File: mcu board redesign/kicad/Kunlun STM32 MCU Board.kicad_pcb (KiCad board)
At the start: 2 copper layers, 40 x 40 mm, 36 parts, among them J1 0532610671, J2 10129383-908001ALF, J3 USB4105-GF-A, J4 5002, J5 5002, J6 5002, J7 5002, J8 5001, J9 5001, SW1 KMR231NG ULC LFS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

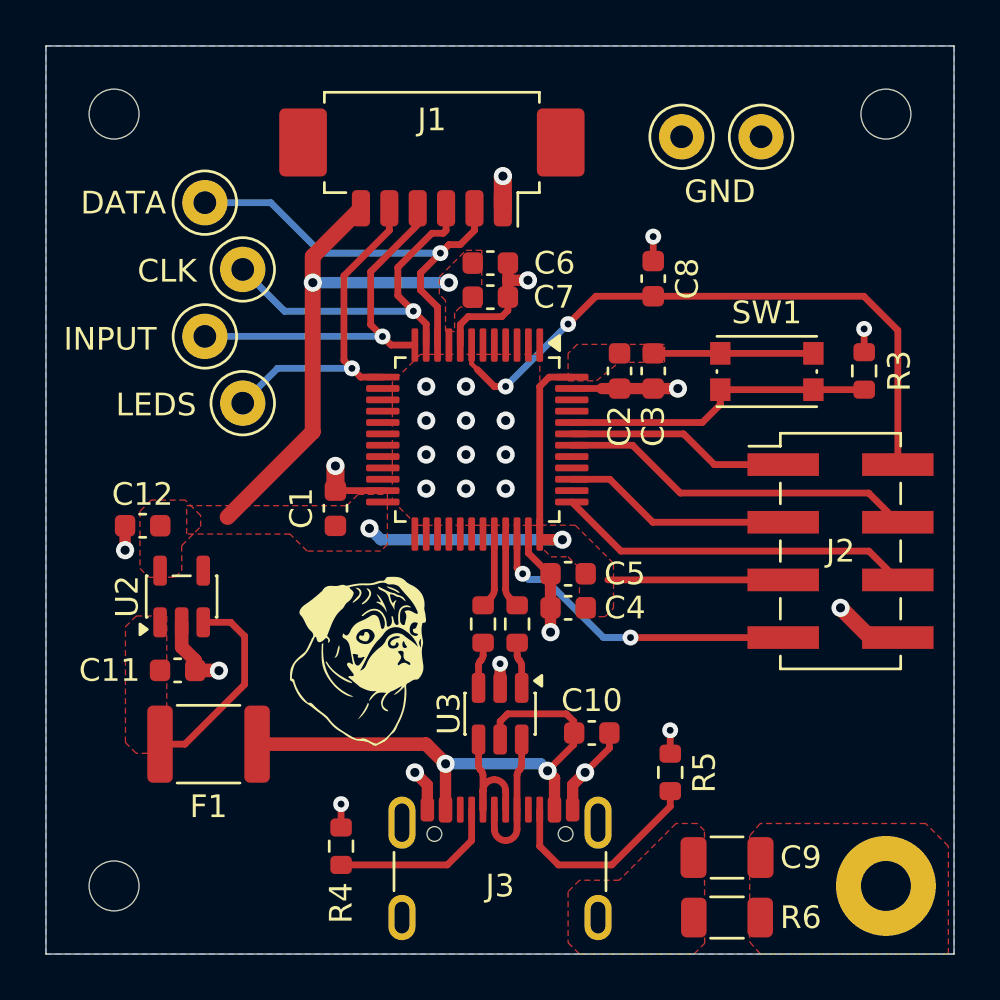
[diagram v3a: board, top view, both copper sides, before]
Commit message: More pretty things
Curve the fill around chassis ground mounting hole.
Label switch as "BOOT"
Pretty up R4
Small trace tweaks
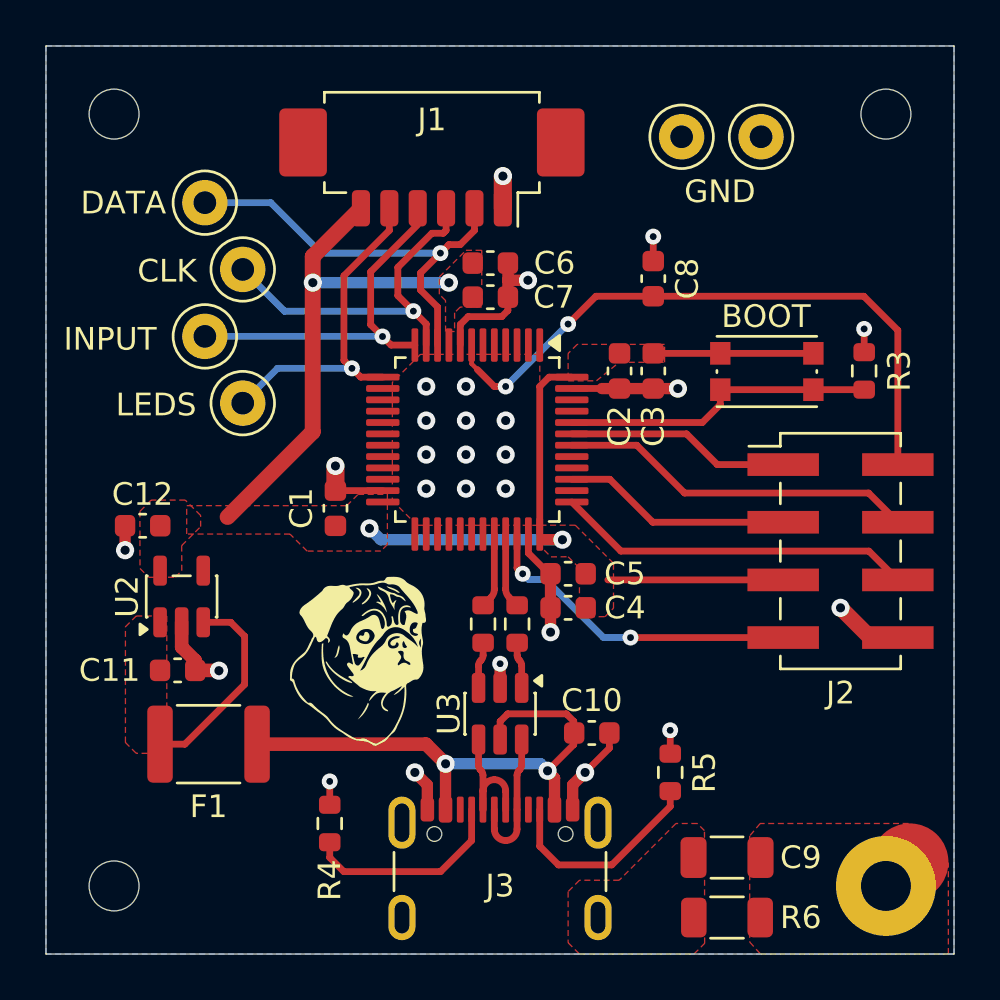
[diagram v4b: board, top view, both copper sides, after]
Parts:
- moved R4 1.12 mm to (140.8, 119.0)
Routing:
- net Net-(J3-CC1): track 7.56 -> 9.11 mm
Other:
- board text added: "BOOT"
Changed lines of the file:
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@@
 		(tags "Surface mounted pin header SMD 2x04 2.54mm double row")
 		(property "Reference" "J2"
-			(at 0 0 0)
+			(at 0 6.25 0)
 			(layer "F.SilkS")
 			(effects
@@
 	(footprint "Resistor_SMD:R_0603_1608Metric"
 		(layer "F.Cu")
-		(at 141.25 120 90)
+		(at 140.75 119 90)
 		(descr "Resistor SMD 0603 (1608 Metric), square (rectangular) end terminal, IPC-7351 nominal, (Body size source: IPC-SM-782 page 72, https://www.pcb-3d.com/wordpress/wp-content/uploads/ipc-sm-782a_amendment_1_and_2.pdf)")
 		(tags "resistor")
@@
 			(at -0.004838 -2.590547 180)
 			(layer "F.SilkS")
+			(hide yes)
 			(effects
 				(font
@@
 		)
 	)
+	(gr_circle
+		(center 166.303358 120.696583)
+		(end 167.903358 120.696583)
+		(stroke
+			(width 0.2)
+			(type solid)
+		)
+		(fill yes)
+		(layer "F.Cu")
+		(net "Net-(C9-Pad1)")
+	)
 	(gr_poly
 		(pts
@@
 		)
 	)
+	(gr_text "BOOT"
+		(at 158 97.25 0)
+		(layer "F.SilkS")
+		(effects
+			(font
+				(size 1 1)
+				(thickness 0.15)
+			)
+			(justify left bottom)
+		)
+	)
 	(gr_text "J2\n1-UART1_RX\n2-NRST\n3-PB3\n4-UART1_TX\n5-VDD\n6-SWCLK\n7-SWDIO\n8-GND"
 		(at 165.25 116.842768 0)
@@
 	)
 	(segment
-		(start 141.249999 118.145384)
-		(end 141.25 119.175)
+		(start 140.749999 117.145384)
+		(end 140.75 118.175)
 		(width 0.3)
 		(layer "F.Cu")
@@
 	)
 	(via
-		(at 141.249999 118.145384)
+		(at 140.749999 117.145384)
 		(size 0.7)
 		(drill 0.3)
@@
 	)
 	(segment
-		(start 156.3375 101.8375)
-		(end 157.69 103.19)
+		(start 156.468086 101.8375)
+		(end 157.820586 103.19)
 		(width 0.3)
 		(layer "F.Cu")
@@
 	(segment
 		(start 151.4125 101.8375)
-		(end 156.3375 101.8375)
+		(end 156.468086 101.8375)
 		(width 0.3)
 		(layer "F.Cu")
@@
 	)
 	(segment
-		(start 157.69 103.19)
+		(start 157.820586 103.19)
 		(end 160.725 103.19)
 		(width 0.3)
@@
 	)
 	(segment
-		(start 164.488488 104.443488)
-		(end 165.775 105.73)
+		(start 154.275773 102.3375)
+		(end 156.381761 104.443488)
 		(width 0.3)
 		(layer "F.Cu")
@@
 	)
 	(segment
-		(start 151.4125 102.3375)
-		(end 154.0875 102.3375)
+		(start 156.381761 104.443488)
+		(end 164.488488 104.443488)
 		(width 0.3)
 		(layer "F.Cu")
@@
 	)
 	(segment
-		(start 154.0875 102.3375)
-		(end 156.193488 104.443488)
+		(start 164.488488 104.443488)
+		(end 165.775 105.73)
 		(width 0.3)
 		(layer "F.Cu")
@@
 	)
 	(segment
-		(start 156.193488 104.443488)
-		(end 164.488488 104.443488)
+		(start 151.4125 102.3375)
+		(end 154.275773 102.3375)
 		(width 0.3)
 		(layer "F.Cu")
@@
 	)
 	(segment
-		(start 141.25 120.825)
-		(end 145.925 120.825)
+		(start 141.370597 121.120597)
+		(end 140.75 120.5)
 		(width 0.3)
 		(layer "F.Cu")
@@
 	(segment
 		(start 147 119.75)
-		(end 147 118.387601)
+		(end 145.629403 121.120597)
+		(width 0.3)
+		(layer "F.Cu")
+		(net "Net-(J3-CC1)")
+	)
+	(segment
+		(start 145.629403 121.120597)
+		(end 141.370597 121.120597)
 		(width 0.3)
 		(layer "F.Cu")
@@
 	)
 	(segment
-		(start 145.925 120.825)
+		(start 147 118.387601)
 		(end 147 119.75)
 		(width 0.3)
@@
 		(net "Net-(J3-CC1)")
 	)
+	(segment
+		(start 140.75 120.5)
+		(end 140.75 119.825)
+		(width 0.3)
+		(layer "F.Cu")
+		(net "Net-(J3-CC1)")
+	)
 	(zone
 		(net "VBUS")
@@
 		(polygon
 			(pts
-				(xy 159.25 124.222504) (xy 159.725229 124.75) (xy 168 124.75) (xy 168 120) (xy 167 119) (xy 159.712842 119.000002)
+				(xy 159.25 124.222504) (xy 159.725229 124.75) (xy 168 124.75) (xy 168 120.75) (xy 166.25 119) (xy 159.712842 119.000002)
 				(xy 159.250001 119.543641)
 			)
